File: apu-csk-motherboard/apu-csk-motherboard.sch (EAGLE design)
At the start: 19 parts, among them U1 DS3231M+TRL

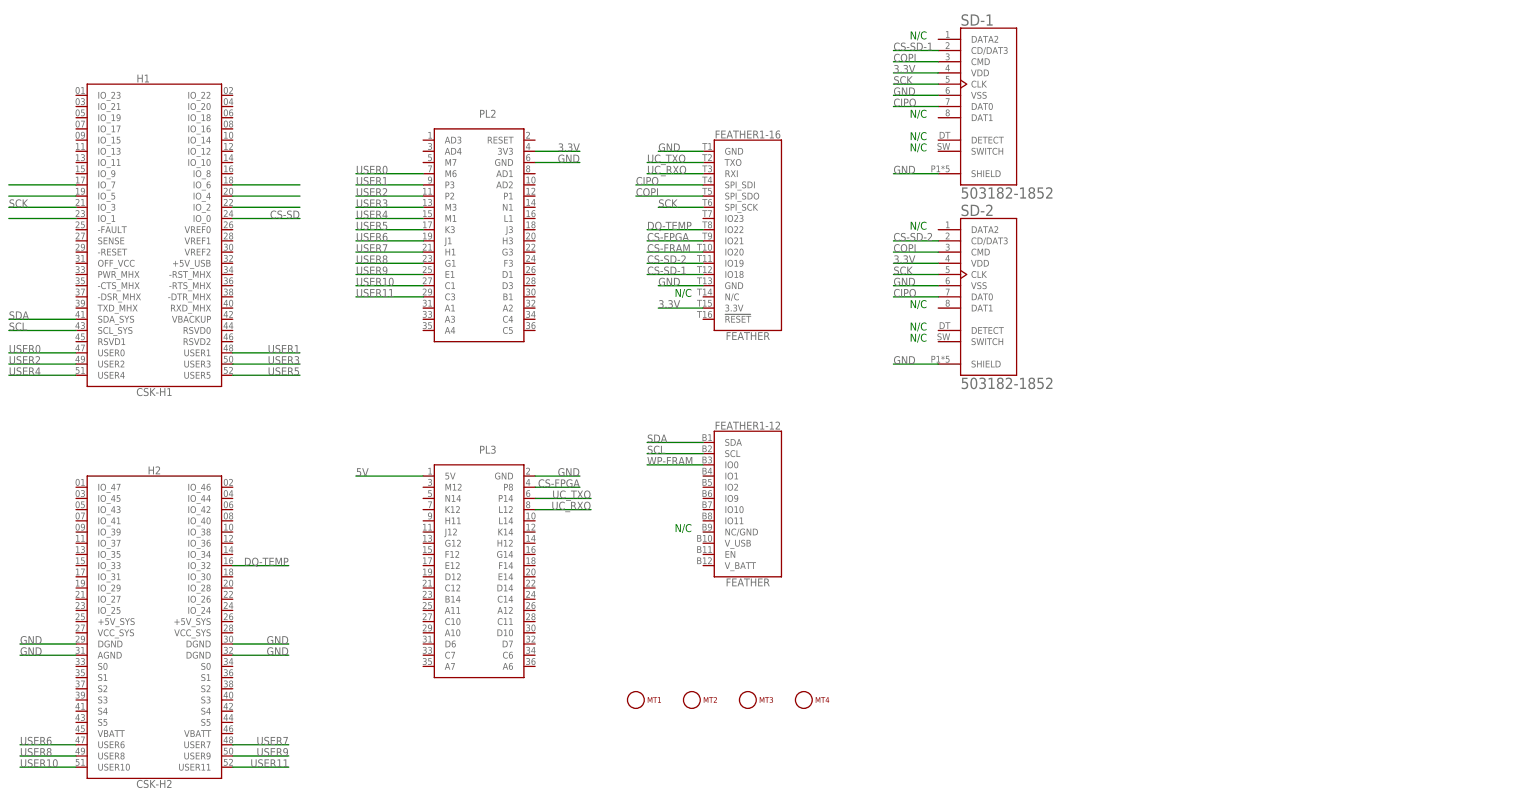
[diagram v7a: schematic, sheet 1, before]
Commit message: Just need to add capacitors
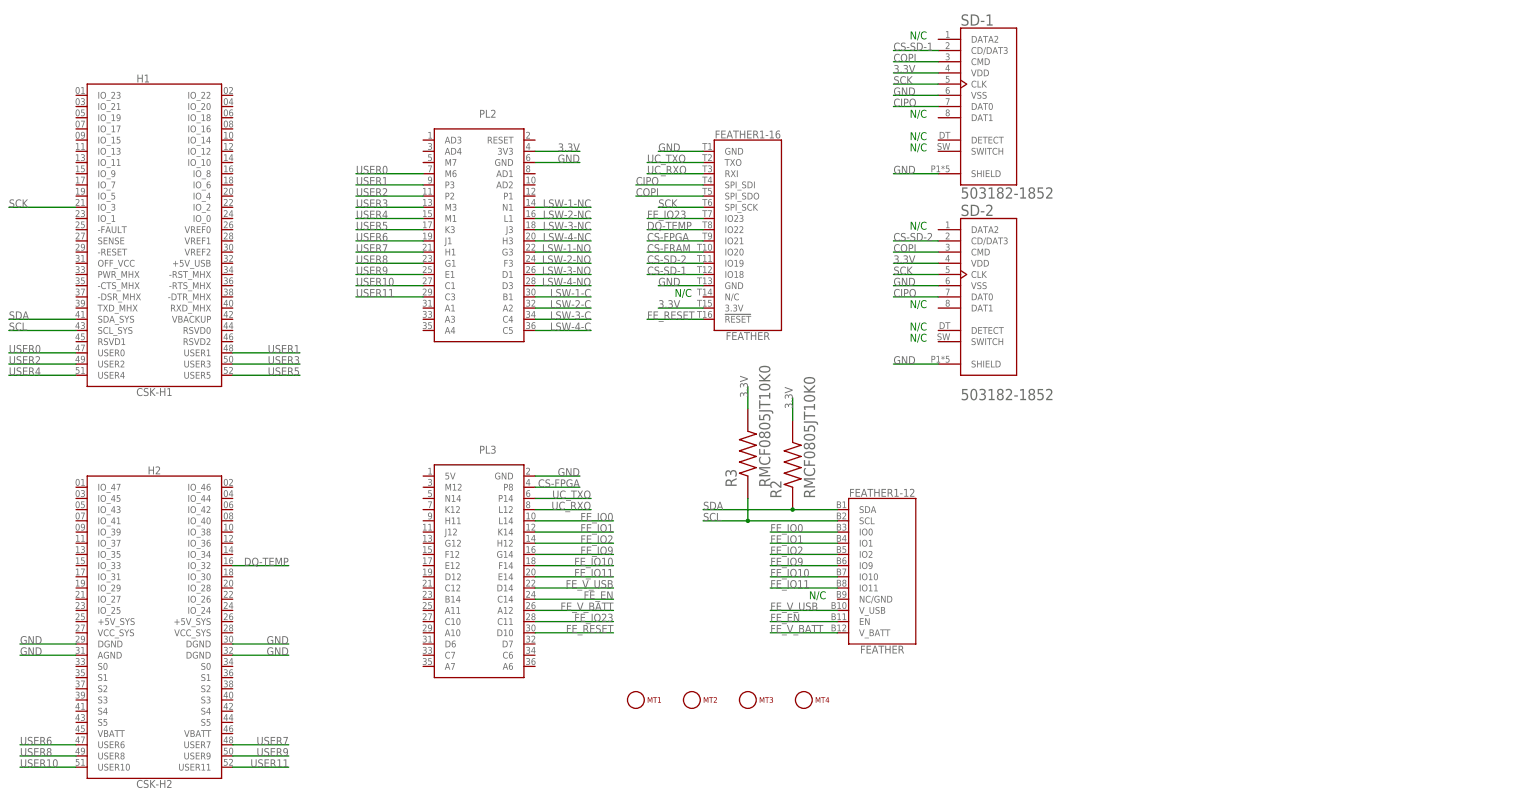
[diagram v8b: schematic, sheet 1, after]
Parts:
- added BT1: BK-890, apu-csk-motherboard:BK-890
- added R2, R3: RMCF0805JT10K0, RMCF0805JT10K0:RMCF0805JT10K0
- AUTHENTICATION-CHIP: device ATECC608A-SSHDA-B:ATECC608A-SSHDA-B -> apu-csk-motherboard:ATECC608A-SSHDA-B
- SD-1, SD-2: device 503182-1852:503182-1852 -> apu-csk-motherboard:503182-1852
- TEMP-SENSE1, TEMP-SENSE2, TEMP-SENSE3, TEMP-SENSE4: device DS18B20:DS18B20 -> apu-csk-motherboard:DS18B20
- U1: device DS3231M_TRL:DS3231M+TRL -> apu-csk-motherboard:DS3231M+TRL
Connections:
- removed net 5V: PL3.5V@1
- removed net CS-SD: H1.IO_0@24
- removed net N$11: U1.!NT/SQW
- removed net N$2: H1.IO_2@22
- removed net N$3: H1.IO_4@20
- removed net N$4: H1.IO_6@18
- removed net N$5: H1.IO_1@23
- removed net N$6: U1.VBAT
- removed net N$7: H1.IO_5@19
- removed net N$8: H1.IO_7@17
- removed net N$9: U1.!RST
- removed net RTCLOCK: U1.32KHZ
- removed net WP-FRAM: FEATHER1-12.IO0@B3, R1.08
- new net FE_EN: FEATHER1-12.EN@B11, PL3.C14@24
- new net FE_IO0: FEATHER1-12.IO0@B3, PL3.L14@10
- new net FE_IO1: FEATHER1-12.IO1@B4, PL3.K14@12
- new net FE_IO10: FEATHER1-12.IO10@B7, PL3.F14@18
- new net FE_IO11: FEATHER1-12.IO11@B8, PL3.E14@20
- new net FE_IO2: FEATHER1-12.IO2@B5, PL3.H12@14
- new net FE_IO23: FEATHER1-16.IO23@T7, PL3.C11@28
- new net FE_IO9: FEATHER1-12.IO9@B6, PL3.G14@16
- new net FE_RESET: FEATHER1-16.!RESET@T16, PL3.D10@30
- new net FE_V_BATT: FEATHER1-12.V_BATT@B12, PL3.A12@26
- new net FE_V_USB: FEATHER1-12.V_USB@B10, PL3.D14@22
- new net N$1: BT1.+, U1.VBAT
- net 3.3V: now also R2.2, R3.2
- net GND: now also BT1.-
- net LSW-1-C: now also PL2.B1@30
- net LSW-1-NC: now also PL2.N1@14
- net LSW-1-NO: now also PL2.G3@22
- net LSW-2-C: now also PL2.A2@32
- net LSW-2-NC: now also PL2.L1@16
- net LSW-2-NO: now also PL2.F3@24
- net LSW-3-C: now also PL2.C4@34
- net LSW-3-NC: now also PL2.J3@18
- net LSW-3-NO: now also PL2.D1@26
- net LSW-4-C: now also PL2.C5@36
- net LSW-4-NC: now also PL2.H3@20
- net LSW-4-NO: now also PL2.D3@28
- net SCL: now also R3.1
- net SDA: now also R2.1
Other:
- moved on the sheet: FEATHER1-12
